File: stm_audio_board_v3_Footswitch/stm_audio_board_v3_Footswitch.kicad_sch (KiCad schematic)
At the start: 2 parts, among them J2 Conn_01x10_Footswitch

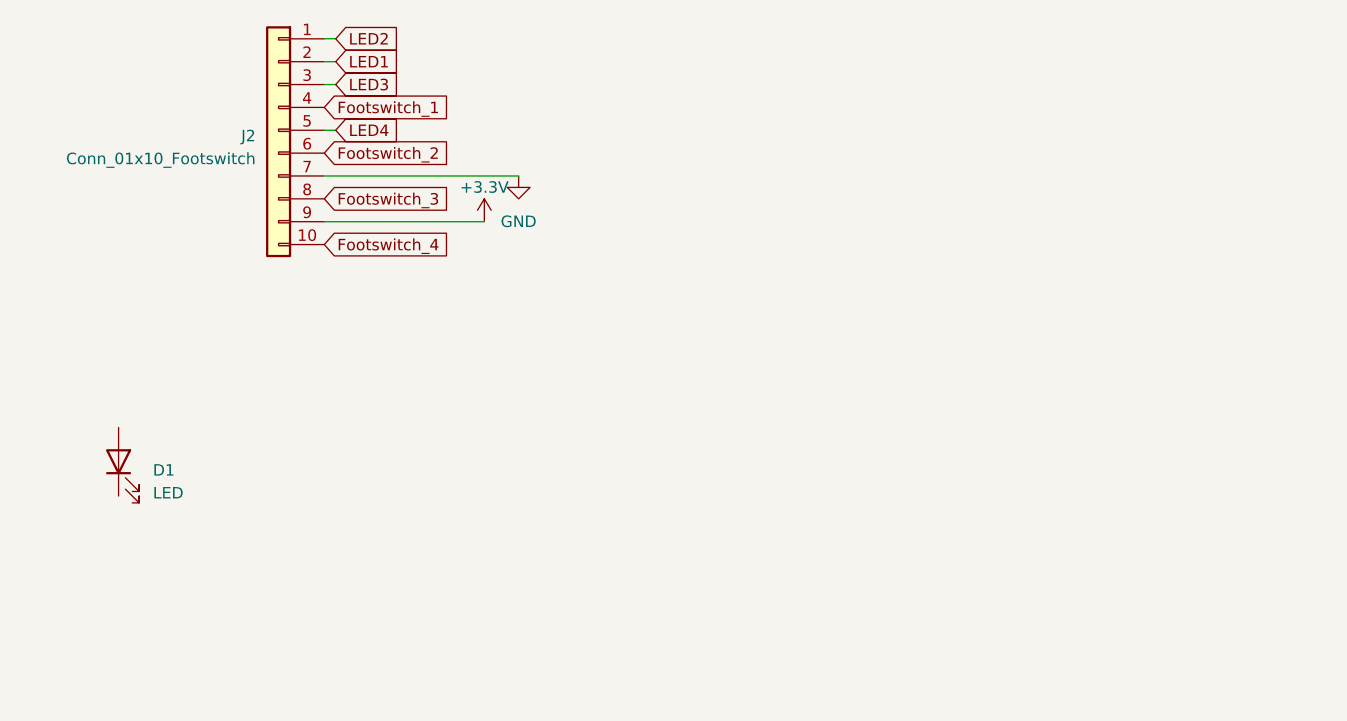
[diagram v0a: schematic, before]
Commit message: Problem with new footprint grid and pin assignements
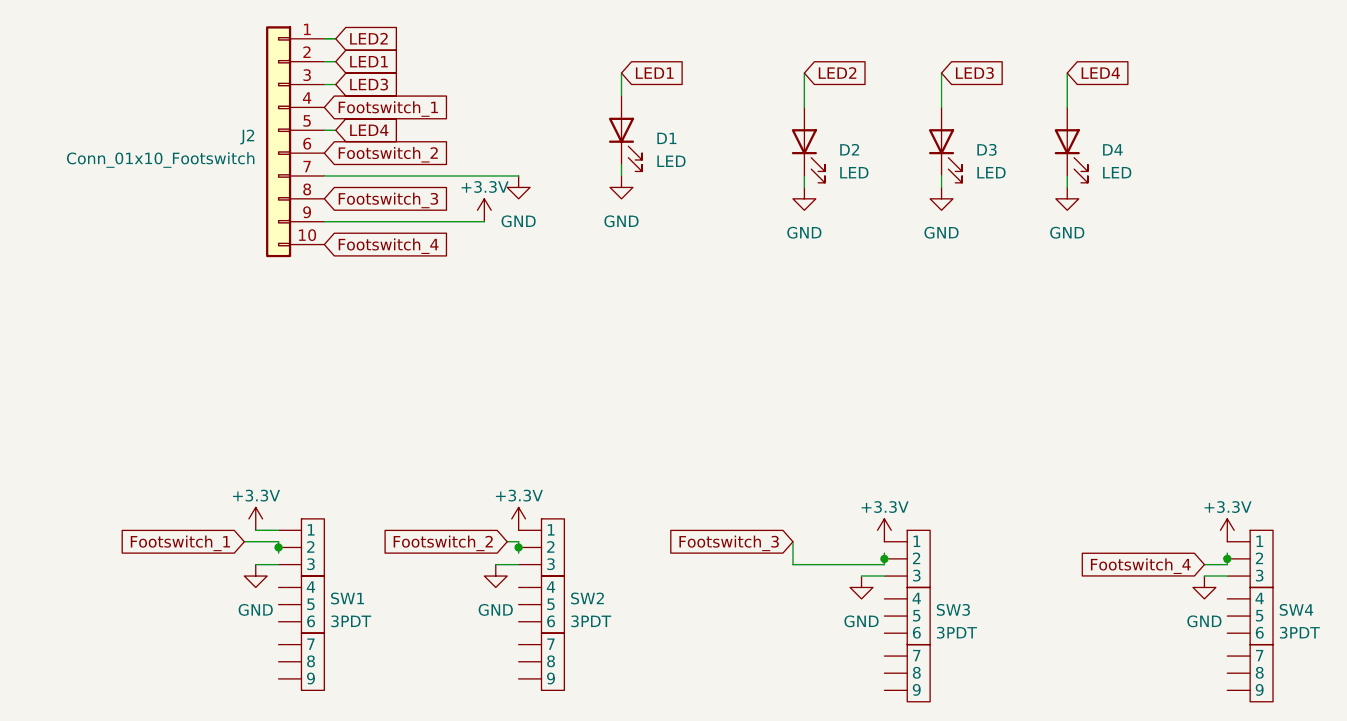
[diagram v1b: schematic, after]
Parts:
- added D2, D3, D4: LED, LED_THT:LED_D5.0mm, symbol Device:LED
- added SW1, SW2, SW3, SW4: 3PDT, switch:3PDT, symbol stm_audio:3PDT
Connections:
- net +3.3V: now also SW1. (9), SW2. (9), SW3. (9), SW4. (9)
- net Footswitch_1: now also SW1. (9)
- net Footswitch_2: now also SW2. (9)
- net Footswitch_3: now also SW3. (9)
- net Footswitch_4: now also SW4. (9)
- net GND: now also D1.1 (K), D2.1 (K), D3.1 (K), D4.1 (K), SW1. (9), SW2. (9), SW3. (9), SW4. (9)
- net LED1: now also D1.2 (A)
- net LED2: now also D2.2 (A)
- net LED3: now also D3.2 (A)
- net LED4: now also D4.2 (A)
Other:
- moved on the sheet: D1

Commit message: updated symbol for 3pdt, created connections
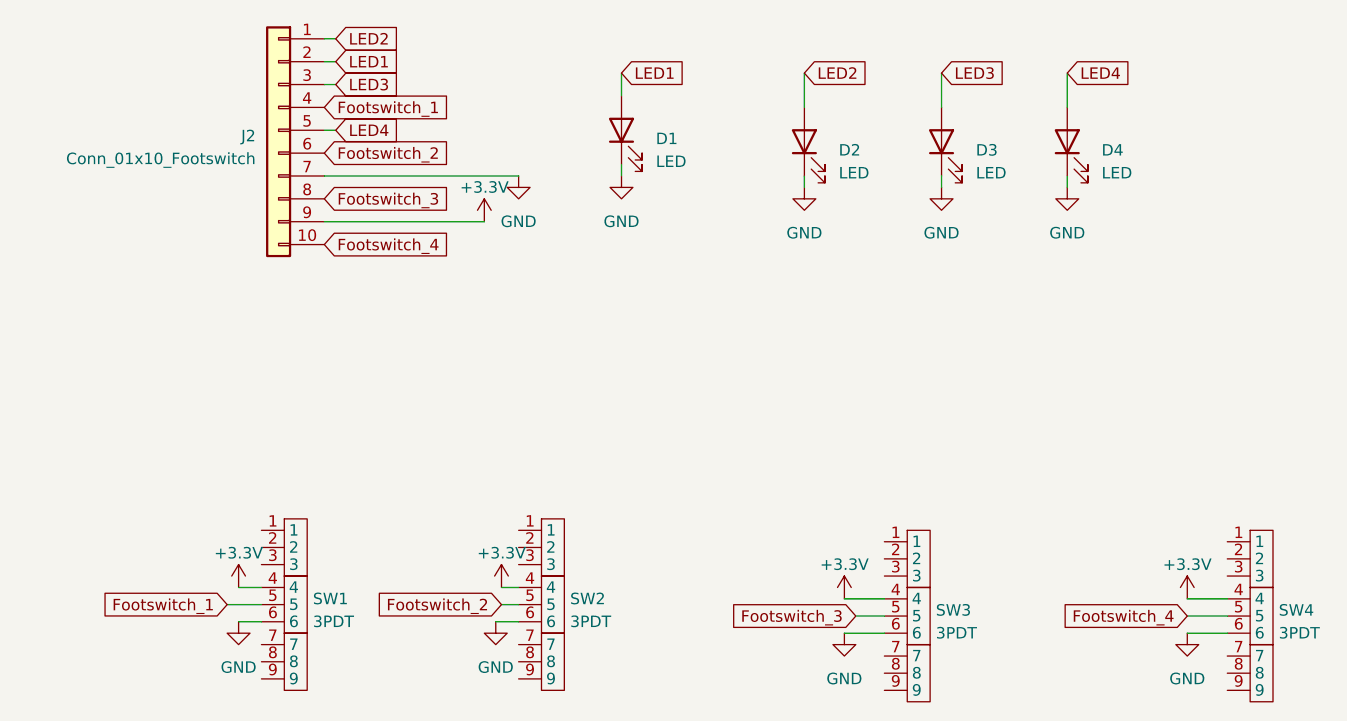
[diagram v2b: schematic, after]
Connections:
- net +3.3V: now also SW1.4, SW2.4, SW3.4, SW4.4; no longer SW1. (9), SW2. (9), SW3. (9), SW4. (9)
- net Footswitch_1: now also SW1.5; no longer SW1. (9)
- net Footswitch_2: now also SW2.5; no longer SW2. (9)
- net Footswitch_3: now also SW3.5; no longer SW3. (9)
- net Footswitch_4: now also SW4.5; no longer SW4. (9)
- net GND: now also SW1.6, SW2.6, SW3.6, SW4.6; no longer SW1. (9), SW2. (9), SW3. (9), SW4. (9)
